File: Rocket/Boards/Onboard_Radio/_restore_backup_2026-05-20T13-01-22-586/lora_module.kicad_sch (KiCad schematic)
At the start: 31 parts, among them J6 RFIO SMA, U2 SX1262, U3 PE4259 RF Switch, Y1 32.000MHz

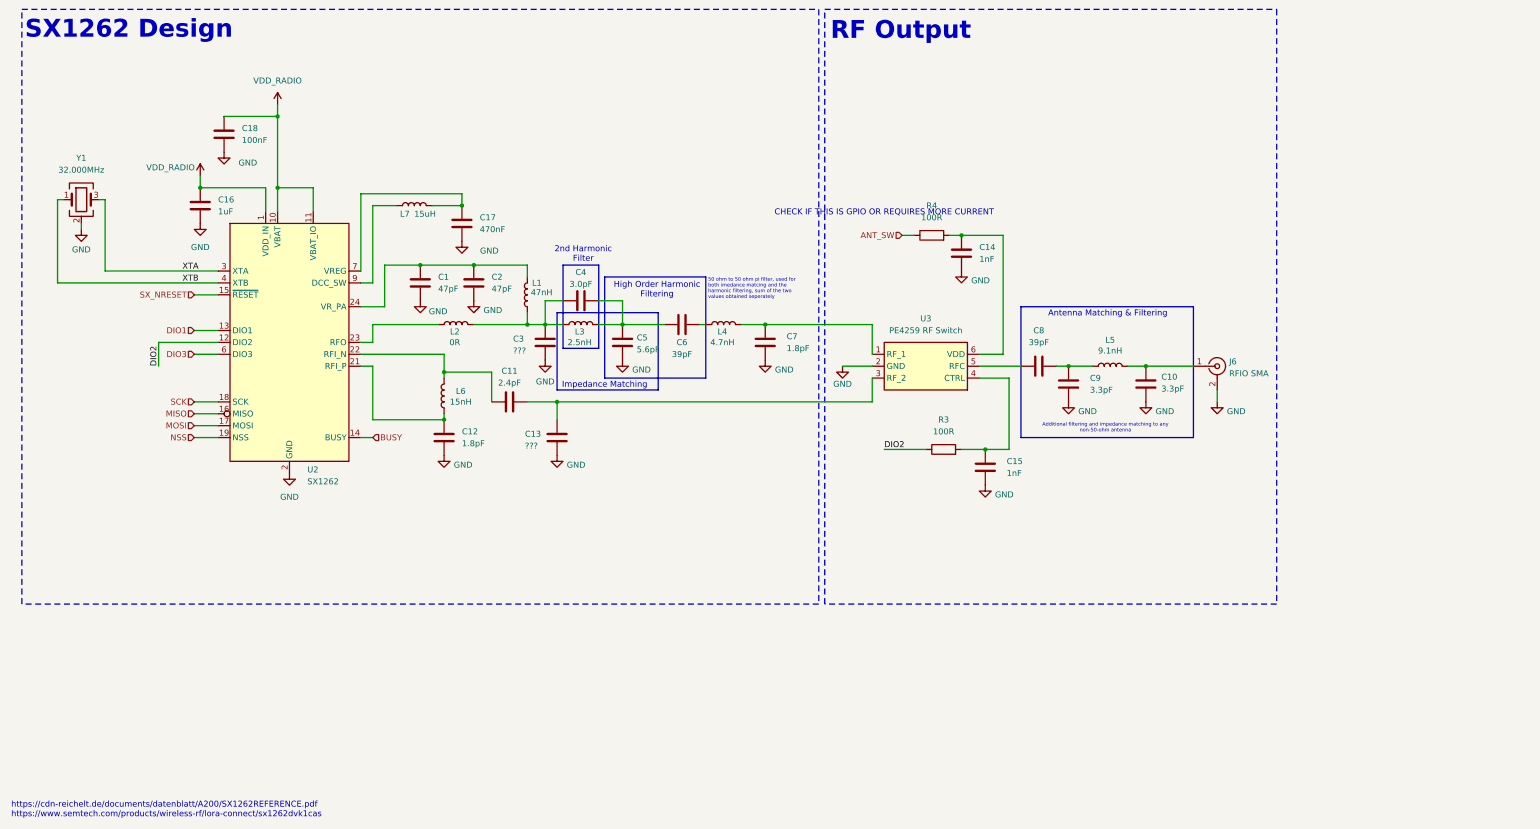
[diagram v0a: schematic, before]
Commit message: schematic bom needs updating and traces need finishing
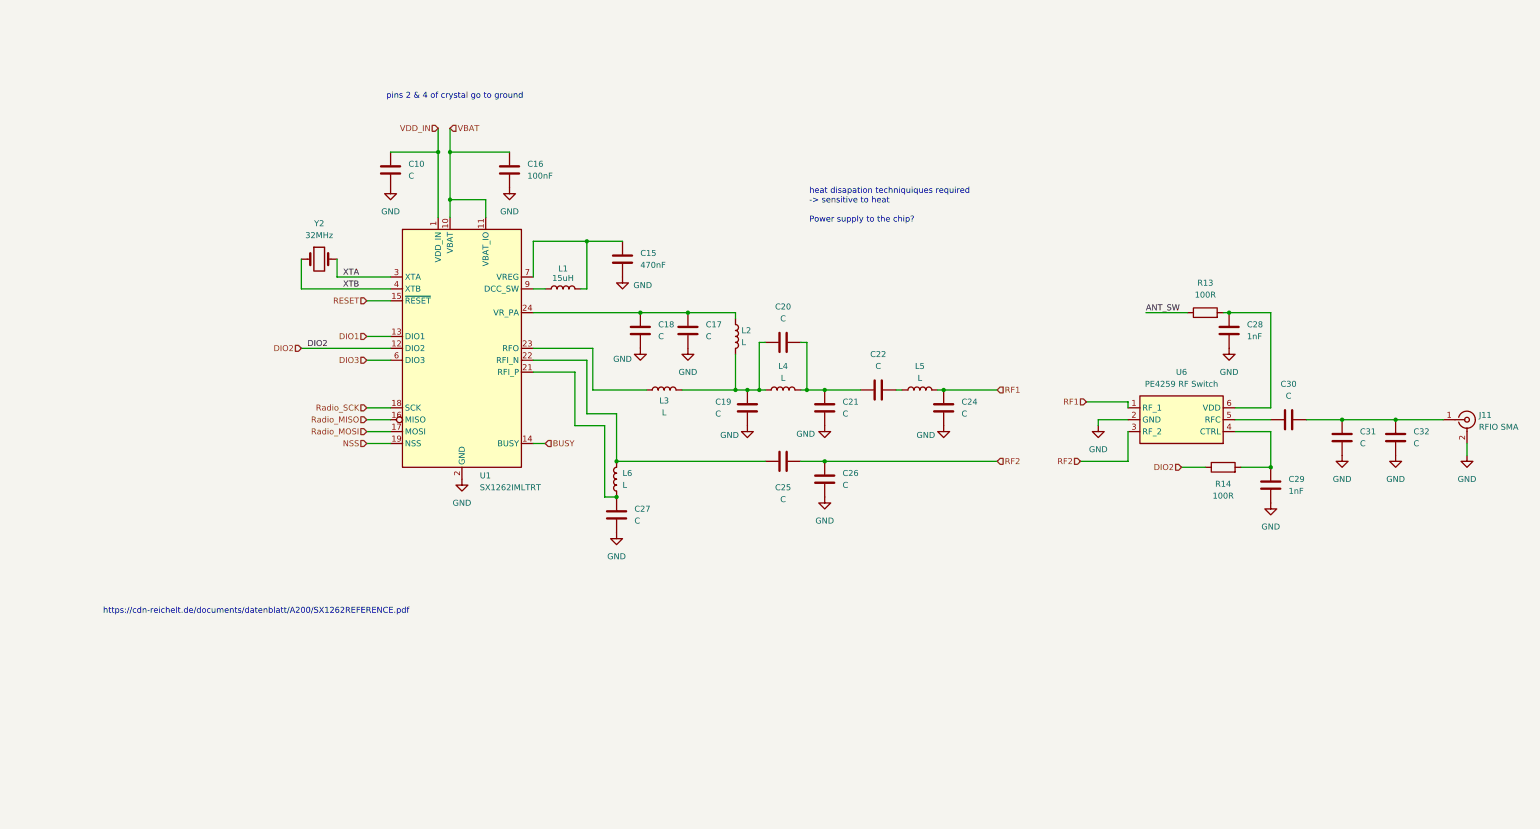
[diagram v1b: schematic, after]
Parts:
- removed C1, C2: 47pF, Capacitor_SMD:C_0402_1005Metric, symbol Device:C
- removed C11: 2.4pF, Capacitor_SMD:C_0402_1005Metric, symbol Device:C
- removed C12, C7: 1.8pF, Capacitor_SMD:C_0402_1005Metric, symbol Device:C
- removed C13, C3: ???, Capacitor_SMD:C_0402_1005Metric, symbol Device:C
- removed C14: 1nF, Capacitor_SMD:C_0402_1005Metric, symbol Device:C
- removed C4: 3.0pF, Capacitor_SMD:C_0402_1005Metric, symbol Device:C
- removed C5: 5.6pF, Capacitor_SMD:C_0402_1005Metric, symbol Device:C
- removed C6, C8: 39pF, Capacitor_SMD:C_0402_1005Metric, symbol Device:C
- removed C9: 3.3pF, Capacitor_SMD:C_0402_1005Metric, symbol Device:C
- removed J6: RFIO SMA, Library:JOHNSON_142-0701-841, symbol Connector:Conn_Coaxial
- removed L7: 15uH, Inductor_SMD:L_0805_2012Metric, symbol Device:L
- removed R3, R4: 100R, Resistor_SMD:R_0402_1005Metric, symbol Device:R
- removed U2: SX1262, Package_DFN_QFN:QFN-24-1EP_4x4mm_P0.5mm_EP2.6x2.6mm, symbol RF:SX1262IMLTRT
- removed U3: PE4259 RF Switch, Package_TO_SOT_SMD:Vishay_PowerPAK_SC70-6L_Dual, symbol Amplifier_Current:NCS213
- removed Y1: 32.000MHz, symbol Device:Crystal_GND24
- added C19, C20, C21, C22, C24, C25, C26, C27, C30, C31, C32: C, Capacitor_SMD:C_0402_1005Metric, symbol Device:C
- added C28, C29: 1nF, Capacitor_SMD:C_0402_1005Metric, symbol Device:C
- added J11: RFIO SMA, symbol Connector:Conn_Coaxial
- added R13, R14: 100R, Resistor_SMD:R_0402_1005Metric, symbol Device:R
- added U1: SX1262IMLTRT, Package_DFN_QFN:QFN-24-1EP_4x4mm_P0.5mm_EP2.6x2.6mm, symbol RF:SX1262IMLTRT
- added U6: PE4259 RF Switch, Package_TO_SOT_SMD:SOT-363_SC-70-6, symbol Amplifier_Current:NCS213
- added Y2: 32MHz, symbol Device:Crystal
- C10: value 3.3pF -> C; MPN GJM1555C1H3R3BB01D -> (none); Manufacturer Murata Electronics -> (none); Max Temp 125 -> (none); Min Temp -55 -> (none); Voltage 50V -> (none)
- C15: value 1nF -> 470nF; MPN GRM155R72A102KA01D -> CL05Y474KP5VPJC; Manufacturer Murata Electronics -> Samsung Electro-Mechanics; Min Temp -55 -> -25; Voltage 100V -> 10V
- C16: value 1uF -> 100nF; MPN GRM155R61C105KA12D -> CL05B104KP5VPNC; Manufacturer Murata Electronics -> Samsung Electro-Mechanics; Max Temp 85 -> 125; Voltage 16V -> 10V
- C17: value 470nF -> C; MPN GRM155R71A474KE01D -> (none); Manufacturer Murata Electronics -> (none); Max Temp 125 -> (none); Min Temp -55 -> (none); Voltage 10V -> (none)
- C18: value 100nF -> C; MPN GRM155R71H104KE14D -> (none); Manufacturer Murata Electronics -> (none); Max Temp -55 -> (none); Min Temp 125 -> (none); Voltage 50V -> (none)
- L1: value 47nH -> 15uH; footprint Inductor_SMD:L_0402_1005Metric -> Library:INDC2012X145N; MPN LQW15AN47NJ00D -> MLZ2012M150WT000; Manufacturer Murata Electronics -> TDK
- L2: value 0R -> L; footprint Resistor_SMD:R_0402_1005Metric -> Library:INDC2012X145N; MPN CRCW04020000Z0ED -> (none); Manufacturer Vishay Dale -> (none); Max Temp 155 -> (none); Min Temp -55 -> (none)
- L3: value 2.5nH -> L; footprint Inductor_SMD:L_0402_1005Metric -> Library:INDC2012X145N; MPN LQW15AN2N5C00D -> (none); Manufacturer Murata Electronics -> (none); Max Temp 125 -> (none); Min Temp -55 -> (none)
- L4: value 4.7nH -> L; footprint Inductor_SMD:L_0402_1005Metric -> Library:INDC2012X145N; MPN LQW15AN4N7C00D -> (none); Manufacturer Murata Electronics -> (none); Max Temp 125 -> (none); Min Temp -55 -> (none)
- L5: value 9.1nH -> L; footprint Inductor_SMD:L_0402_1005Metric -> Library:INDC2012X145N; MPN LQW15AN9N1H00D -> (none); Manufacturer Murata Electronics -> (none); Max Temp 125 -> (none); Min Temp -55 -> (none)
- L6: value 15nH -> L; footprint Inductor_SMD:L_0402_1005Metric -> Library:INDC2012X145N; MPN LQW15AN15NH00D -> (none); Manufacturer Murata Electronics -> (none); Max Temp 125 -> (none); Min Temp -55 -> (none)
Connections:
- net ANT_SW: now also R13.1
- net BUSY: now also U1.14 (BUSY)
- net DIO1: now also U1.13 (DIO1)
- net DIO2: now also R14.1, U1.12 (DIO2)
- net DIO3: now also U1.6 (DIO3)
- net GND: now also C19.2, C21.2, C24.2, C26.1, C27.1, C28.2, C29.2, C31.2, C32.2, J11.2 (Ext), U1.2 (GND), U1.20 (GND), U1.25 (GND), U1.5 (GND), U1.8 (GND), U6.2 (GND)
- net NSS: now also U1.19 (NSS)
- net XTA: now also U1.3 (XTA), Y2.2
- net XTB: now also U1.4 (XTB), Y2.1
- net at L6.1: now also C27.2, U1.21 (RFI_P)
- net at L6.2: now also C25.1, U1.22 (RFI_N)
- net at L2.1: now also C17.1, C18.1, U1.24 (VR_PA)
- net at L1.2: now also C15.1, U1.7 (VREG)
- net at L5.1: now also C22.2
- net at L3.2: now also L2.2, L4.1, C19.1, C20.1
- net at L4.2: now also C20.2, C21.1, C22.1
- net RF1: now reaches L5.2
- net RF1: now also C24.1, U6.1 (RF_1); no longer C10.1
- net VDD_RADIO renamed VBAT
- net VBAT: now also U1.10 (VBAT), U1.11 (VBAT_IO); no longer C18.1
- new net: C28.1, R13.2, U6.6 (VDD)
- new net: L3.1, U1.23 (RFO)
- new net: L1.1, U1.9 (DCC_SW)
- new net: C29.1, R14.2, U6.4 (CTRL)
- new net: C30.1, U6.5 (RFC)
- new net: C30.2, C31.1, C32.1, J11.1 (In)
- new net RESET: U1.15 (~{RESET})
- new net RF2: C25.2, C26.2, U6.3 (RF_2)
- new net Radio_MISO: U1.16 (MISO)
- new net Radio_MOSI: U1.17 (MOSI)
- new net Radio_SCK: U1.18 (SCK)
- new net VDD_IN: C10.1, U1.1 (VDD_IN)
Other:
- note added: "heat disapation techniquiques required -> sensitive to heat Power supply to the chip?"
- note added: "https://cdn-reichelt.de/documents/datenblatt/A200/SX1262REFERENCE.pdf"
- note added: "pins 2 & 4 of crystal go to ground"
- note removed: "2nd Harmonic Filter"
- note removed: "50 ohm to 50 ohm pi filter, used for both imedance matcing and the harmonic filtering, sum of the two values obtained seperately"
- note removed: "Additional filtering and impedance matching to any non-50-ohm antenna"
- note removed: "Antenna Matching & Filtering"
- note removed: "CHECK IF THIS IS GPIO OR REQUIRES MORE CURRENT"
- note removed: "High Order Harmonic Filtering"
- note removed: "Impedance Matching"
- note removed: "RF Output"
- note removed: "SX1262 Design"
- note removed: "https://cdn-reichelt.de/documents/datenblatt/A200/SX1262REFERENCE.pdf https://www.semtech.com/products/wireless-rf/lora-connect/sx1262dvk1cas"
